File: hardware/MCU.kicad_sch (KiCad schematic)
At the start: 21 parts, among them J801 UART1, SW801 SW_Push, U801 NUCLEO-L432KC, U802 TCAN1043A, U803 TLP241A

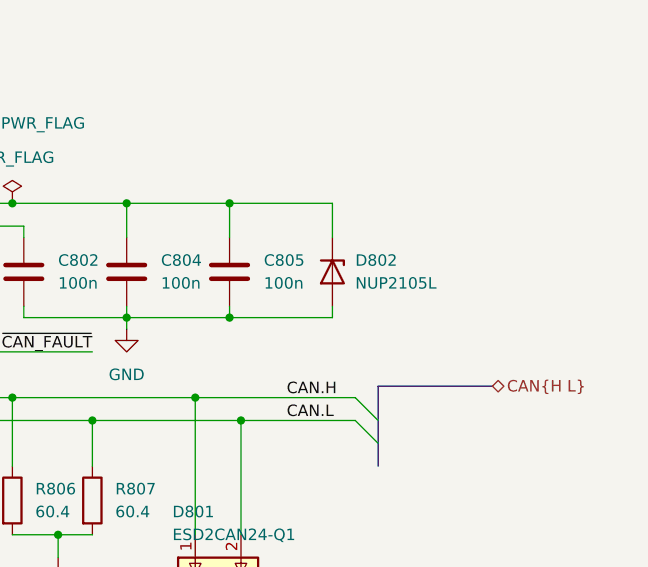
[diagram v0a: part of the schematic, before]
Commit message: Replace CAN TVS D802 (NUP2105L) with PESD1CAN
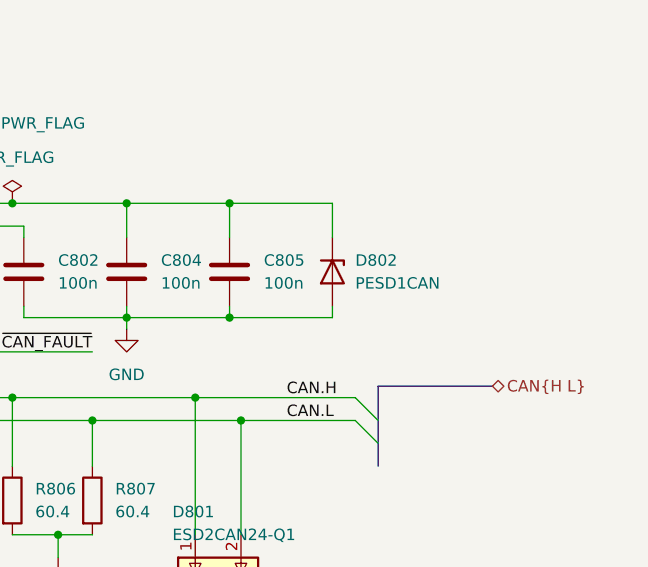
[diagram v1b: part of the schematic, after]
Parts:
- D802: value NUP2105L -> PESD1CAN; LCSC C5158054 -> C2687121

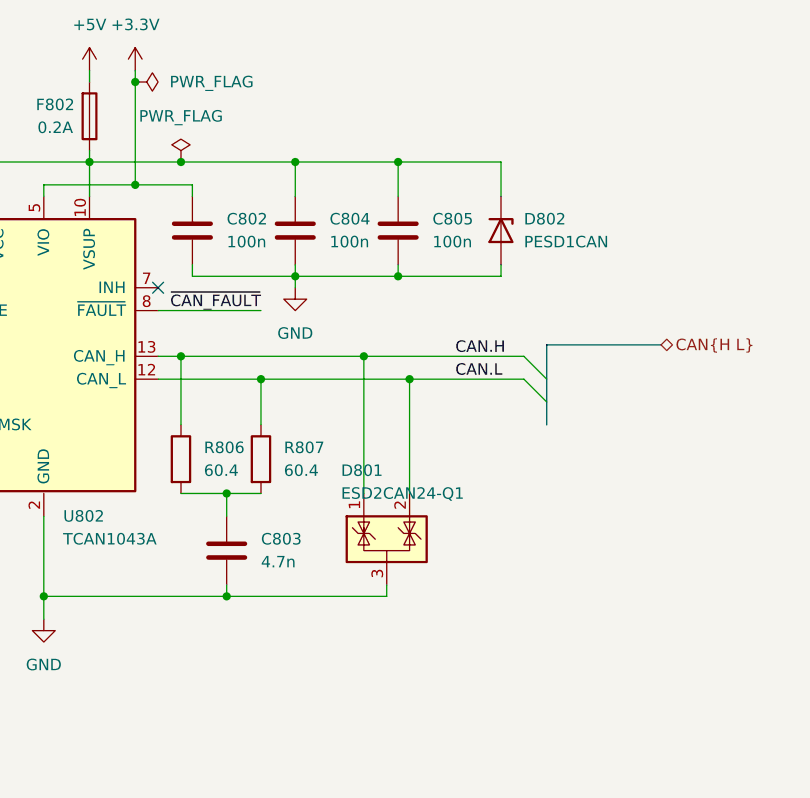
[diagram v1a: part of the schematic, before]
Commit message: added qulon zone
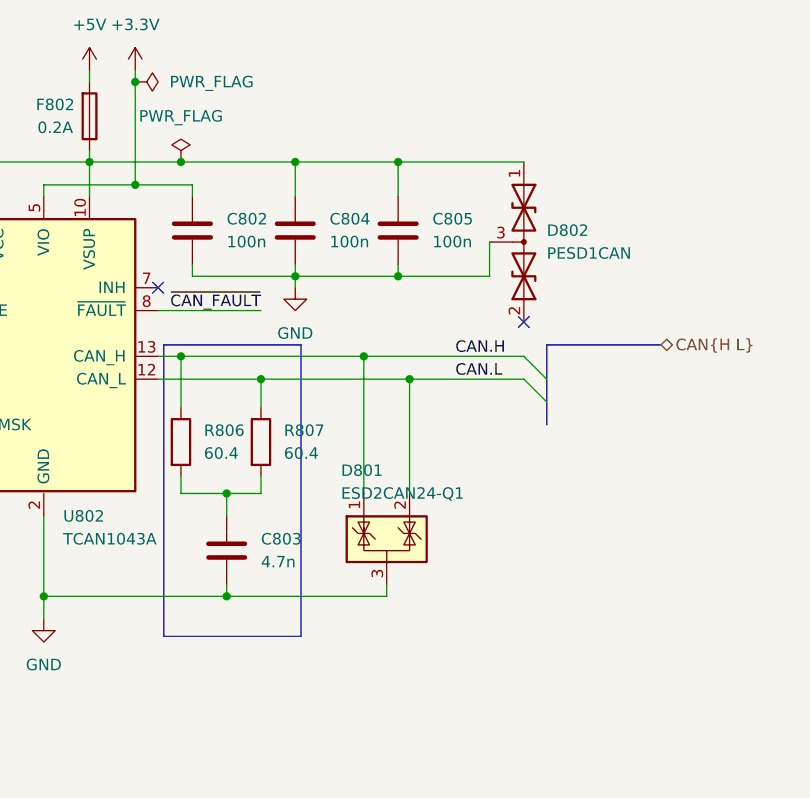
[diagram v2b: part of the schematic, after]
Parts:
- D802: symbol Device:D_Zener -> Device:D_TVS_Dual_AAC
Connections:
- net GND: now also D802.3 (common); no longer D802.2 (A)
- no-connect marks 12 -> 13
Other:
- moved on the sheet: R806, R807

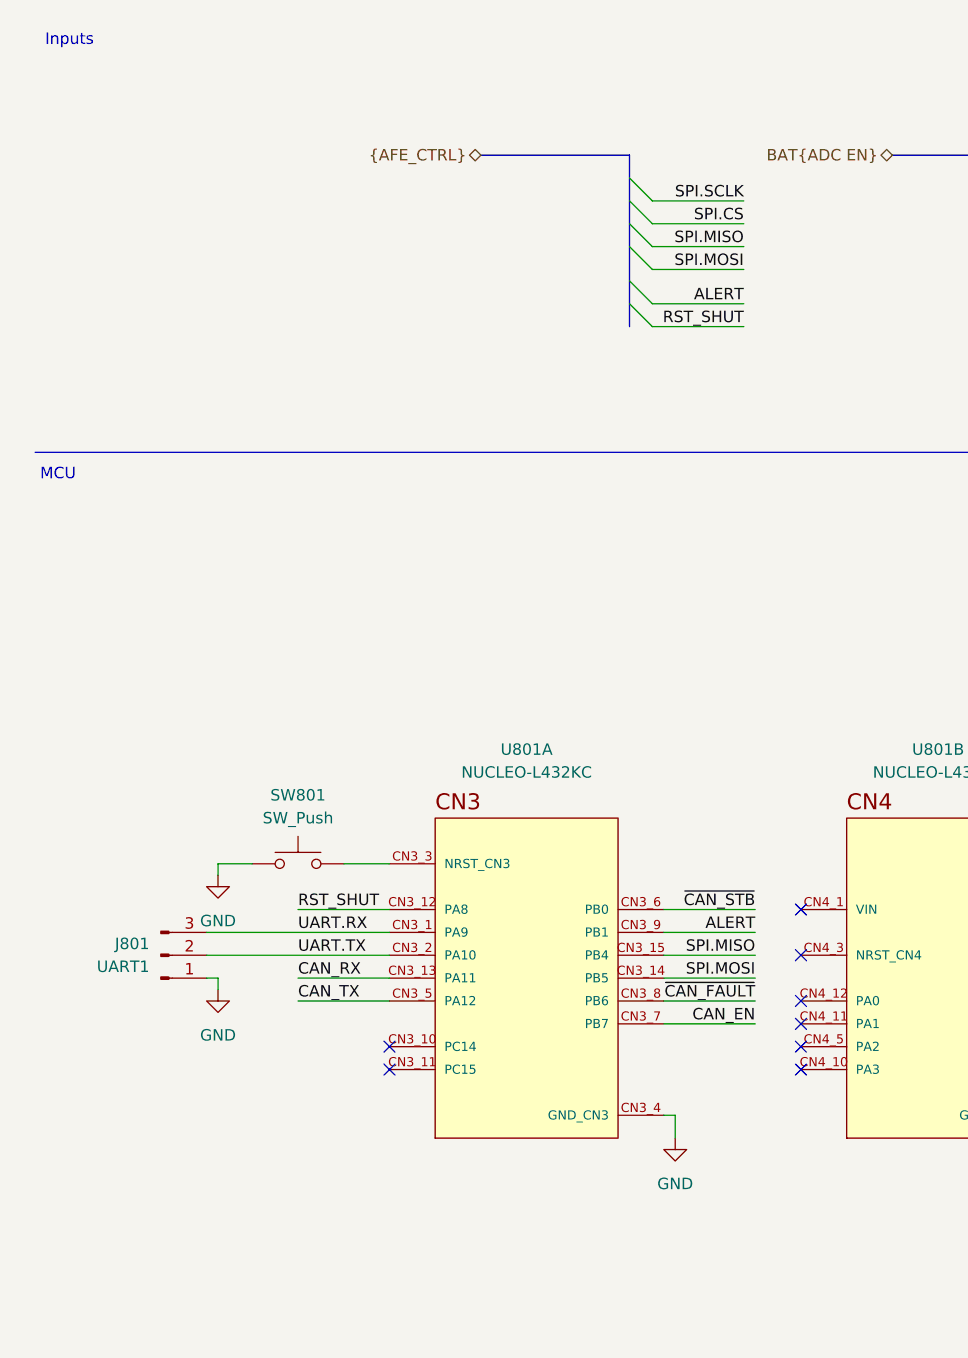
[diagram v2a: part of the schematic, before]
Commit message: move controll signals to back
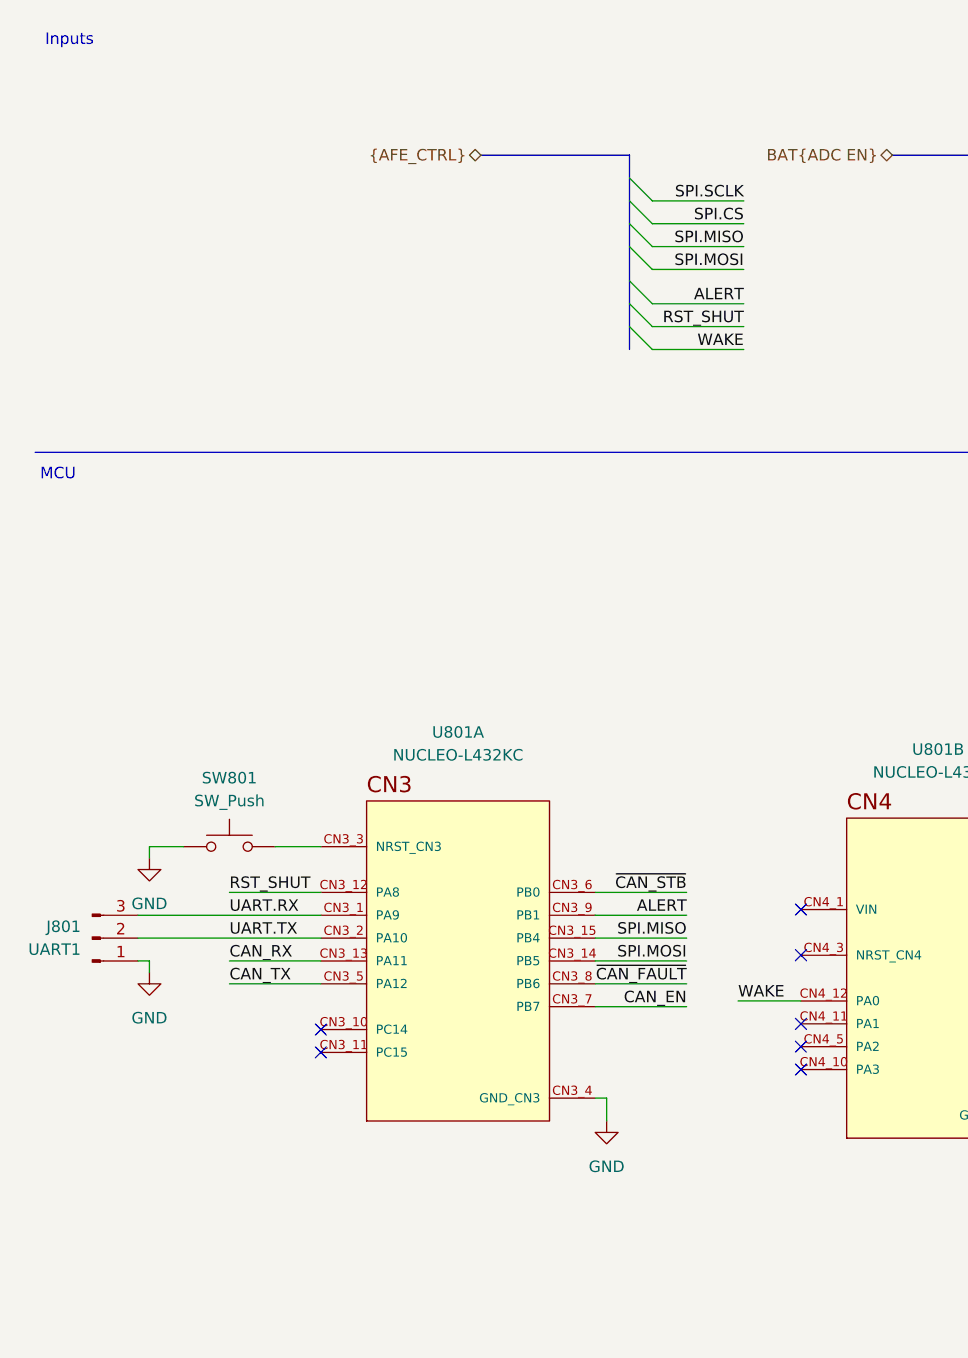
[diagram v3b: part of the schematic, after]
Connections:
- net WAKE: now reaches U801.CN4_12 (PA0)
- no-connect marks 13 -> 12
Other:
- moved on the sheet: J801, SW801, U801A
